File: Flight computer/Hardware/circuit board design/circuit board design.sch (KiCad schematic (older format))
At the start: 0 parts

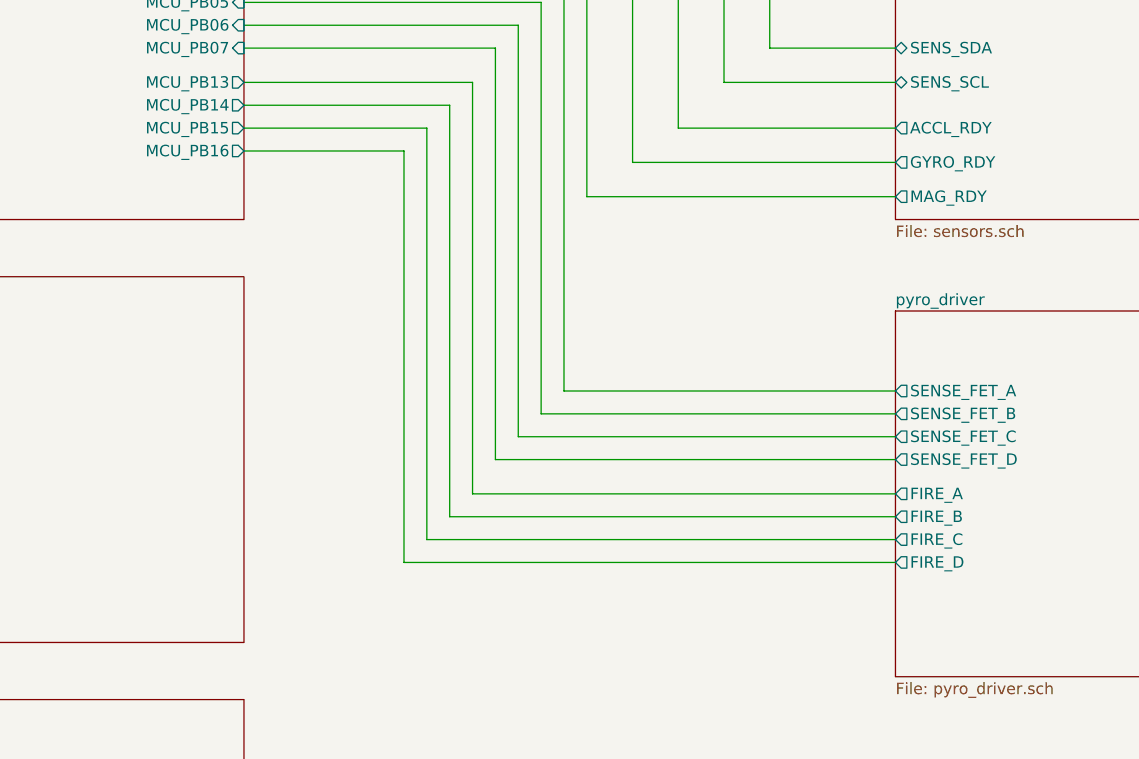
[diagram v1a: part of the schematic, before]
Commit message: added the arming switch. Changed foot print of lipo connector to JST
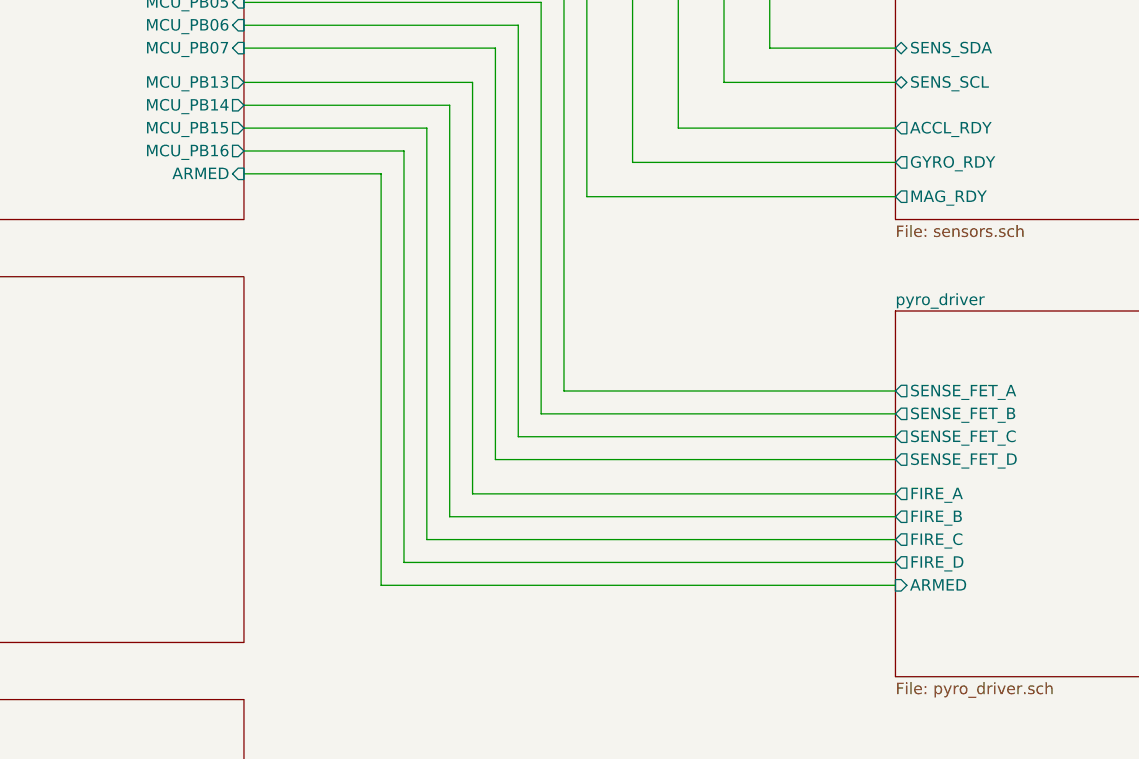
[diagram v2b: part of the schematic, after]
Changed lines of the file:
@@
 F29 "USB_DP" I L 2700 1500 50
 F30 "USB_DM" I L 2700 1400 50
+F31 "ARMED" I R 5050 4100 50
 $EndSheet
 Wire Wire Line
@@
 F8 "SENSE_FET_D" O L 7900 5350 50
 F9 "FIRE_D" O L 7900 5800 50
+F10 "ARMED" I L 7900 5900 50
 $EndSheet
 Wire Wire Line
@@
 Wire Wire Line
 	5050 3550 6150 3550
+Wire Wire Line
+	7900 5900 5650 5900
+Wire Wire Line
+	5650 5900 5650 4100
+Wire Wire Line
+	5650 4100 5050 4100
 $EndSCHEMATC

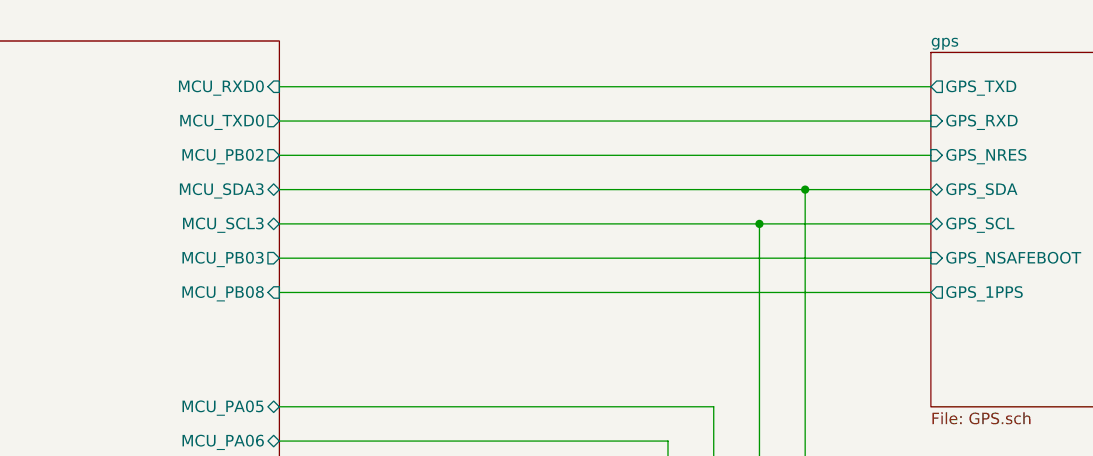
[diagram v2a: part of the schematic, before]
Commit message: changed the SERCOM ports/pins for SPI flash and radio
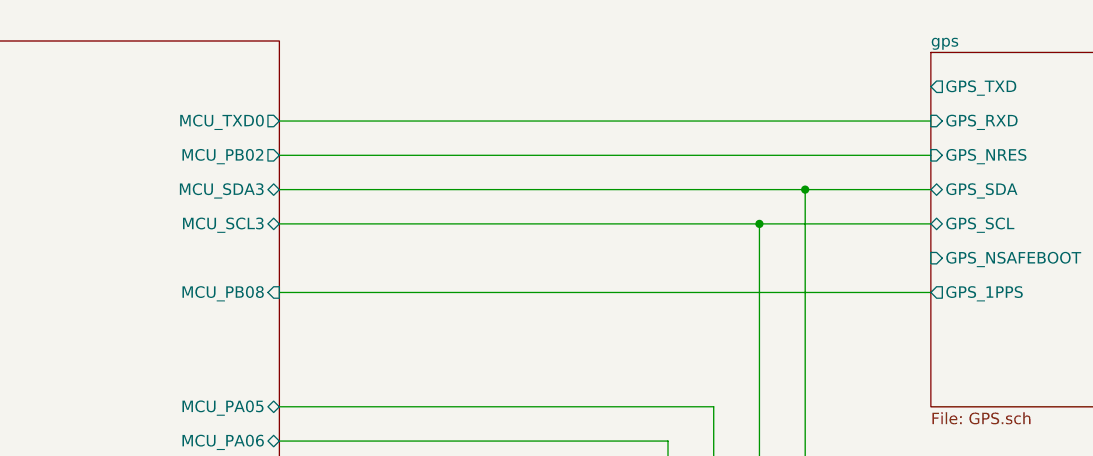
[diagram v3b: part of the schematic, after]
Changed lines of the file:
@@
 	7150 1900 7900 1900
-Wire Wire Line
-	7900 3900 6950 3900
 Wire Wire Line
 	2700 5700 1650 5700
@@
 $EndSheet
 Wire Wire Line
-	7900 4050 6750 4050
-Wire Wire Line
-	6550 3000 6550 4200
-Wire Wire Line
-	6750 4050 6750 2850
-Wire Wire Line
-	6950 3900 6950 2700
-Wire Wire Line
-	6550 4200 7900 4200
-Wire Wire Line
 	6450 3250 6450 5050
 Wire Wire Line
@@
 	5050 1600 7900 1600
 Wire Wire Line
-	5050 2050 7900 2050
-Wire Wire Line
-	5050 3000 6550 3000
-Wire Wire Line
-	6750 2850 5050 2850
-Wire Wire Line
-	6950 2700 5050 2700
-Wire Wire Line
-	7900 1300 5050 1300
-Wire Wire Line
 	5050 1450 7900 1450
 Wire Wire Line
@@
 Wire Wire Line
 	2450 3300 2450 4950
-$Sheet
-S 2700 1100 2350 3200
-U 5D5B15F7
-F0 "MCU" 50
-F1 "MCU.sch" 50
-F2 "MCU_MOSI1" O L 2700 3000 50
-F3 "MCU_SCLK1" O L 2700 3150 50
-F4 "MCU_NSEL1" I L 2700 3300 50
-F5 "MCU_MISO1" O L 2700 2850 50
-F6 "MCU_SDA3" B R 5050 1750 50
-F7 "MCU_SCL3" B R 5050 1900 50
-F8 "MCU_TXD0" O R 5050 1450 50
-F9 "MCU_RXD0" I R 5050 1300 50
-F10 "MCU_PA02" I L 2700 1600 50
-F11 "MCU_PA05" B R 5050 2700 50
-F12 "MCU_PA06" B R 5050 2850 50
-F13 "MCU_PA07" B R 5050 3000 50
-F14 "MCU_PA09" O L 2700 2700 50
-F15 "MCU_PB03" O R 5050 2050 50
-F16 "MCU_PB02" O R 5050 1600 50
-F17 "MCU_PB08" I R 5050 2200 50
-F18 "MCU_PA20" I L 2700 2250 50
-F19 "MCU_PA21" I L 2700 2400 50
-F20 "MCU_PA27" I L 2700 2550 50
-F21 "MCU_PB04" I R 5050 3250 50
-F22 "MCU_PB05" I R 5050 3350 50
-F23 "MCU_PB13" O R 5050 3700 50
-F24 "MCU_PB14" O R 5050 3800 50
-F25 "MCU_PB06" I R 5050 3450 50
-F26 "MCU_PB07" I R 5050 3550 50
-F27 "MCU_PB15" O R 5050 3900 50
-F28 "MCU_PB16" O R 5050 4000 50
-F29 "USB_DP" I L 2700 1500 50
-F30 "USB_DM" I L 2700 1400 50
-F31 "ARMED" I R 5050 4100 50
-$EndSheet
 Wire Wire Line
 	1650 2550 2700 2550
@@
 Wire Wire Line
 	5650 4100 5050 4100
+$Sheet
+S 2700 1100 2350 3200
+U 5D5B15F7
+F0 "MCU" 50
+F1 "MCU.sch" 50
+F2 "MCU_MOSI1" O L 2700 3000 50
+F3 "MCU_SCLK1" O L 2700 3150 50
+F4 "MCU_NSEL1" I L 2700 3300 50
+F5 "MCU_MISO1" O L 2700 2850 50
+F6 "MCU_SDA3" B R 5050 1750 50
+F7 "MCU_SCL3" B R 5050 1900 50
+F8 "MCU_TXD0" O R 5050 1450 50
+F9 "MCU_PA02" I L 2700 1600 50
+F10 "MCU_PA05" B R 5050 2700 50
+F11 "MCU_PA06" B R 5050 2850 50
+F12 "MCU_PA07" B R 5050 3000 50
+F13 "MCU_PA09" O L 2700 2700 50
+F14 "MCU_PB02" O R 5050 1600 50
+F15 "MCU_PB08" I R 5050 2200 50
+F16 "MCU_PA20" I L 2700 2250 50
+F17 "MCU_PA21" I L 2700 2400 50
+F18 "MCU_PA27" I L 2700 2550 50
+F19 "MCU_PB04" I R 5050 3250 50
+F20 "MCU_PB05" I R 5050 3350 50
+F21 "MCU_PB13" O R 5050 3700 50
+F22 "MCU_PB14" O R 5050 3800 50
+F23 "MCU_PB06" I R 5050 3450 50
+F24 "MCU_PB07" I R 5050 3550 50
+F25 "MCU_PB15" O R 5050 3900 50
+F26 "MCU_PB16" O R 5050 4000 50
+F27 "USB_DP" I L 2700 1500 50
+F28 "USB_DM" I L 2700 1400 50
+F29 "ARMED" I R 5050 4100 50
+$EndSheet
+Wire Wire Line
+	6550 4200 7900 4200
+Wire Wire Line
+	6950 3900 6950 2700
+Wire Wire Line
+	6750 4050 6750 2850
+Wire Wire Line
+	6550 3000 6550 4200
+Wire Wire Line
+	7900 4050 6750 4050
+Wire Wire Line
+	7900 3900 6950 3900
+Wire Wire Line
+	6950 2700 5050 2700
+Wire Wire Line
+	6750 2850 5050 2850
+Wire Wire Line
+	5050 3000 6550 3000
 $EndSCHEMATC

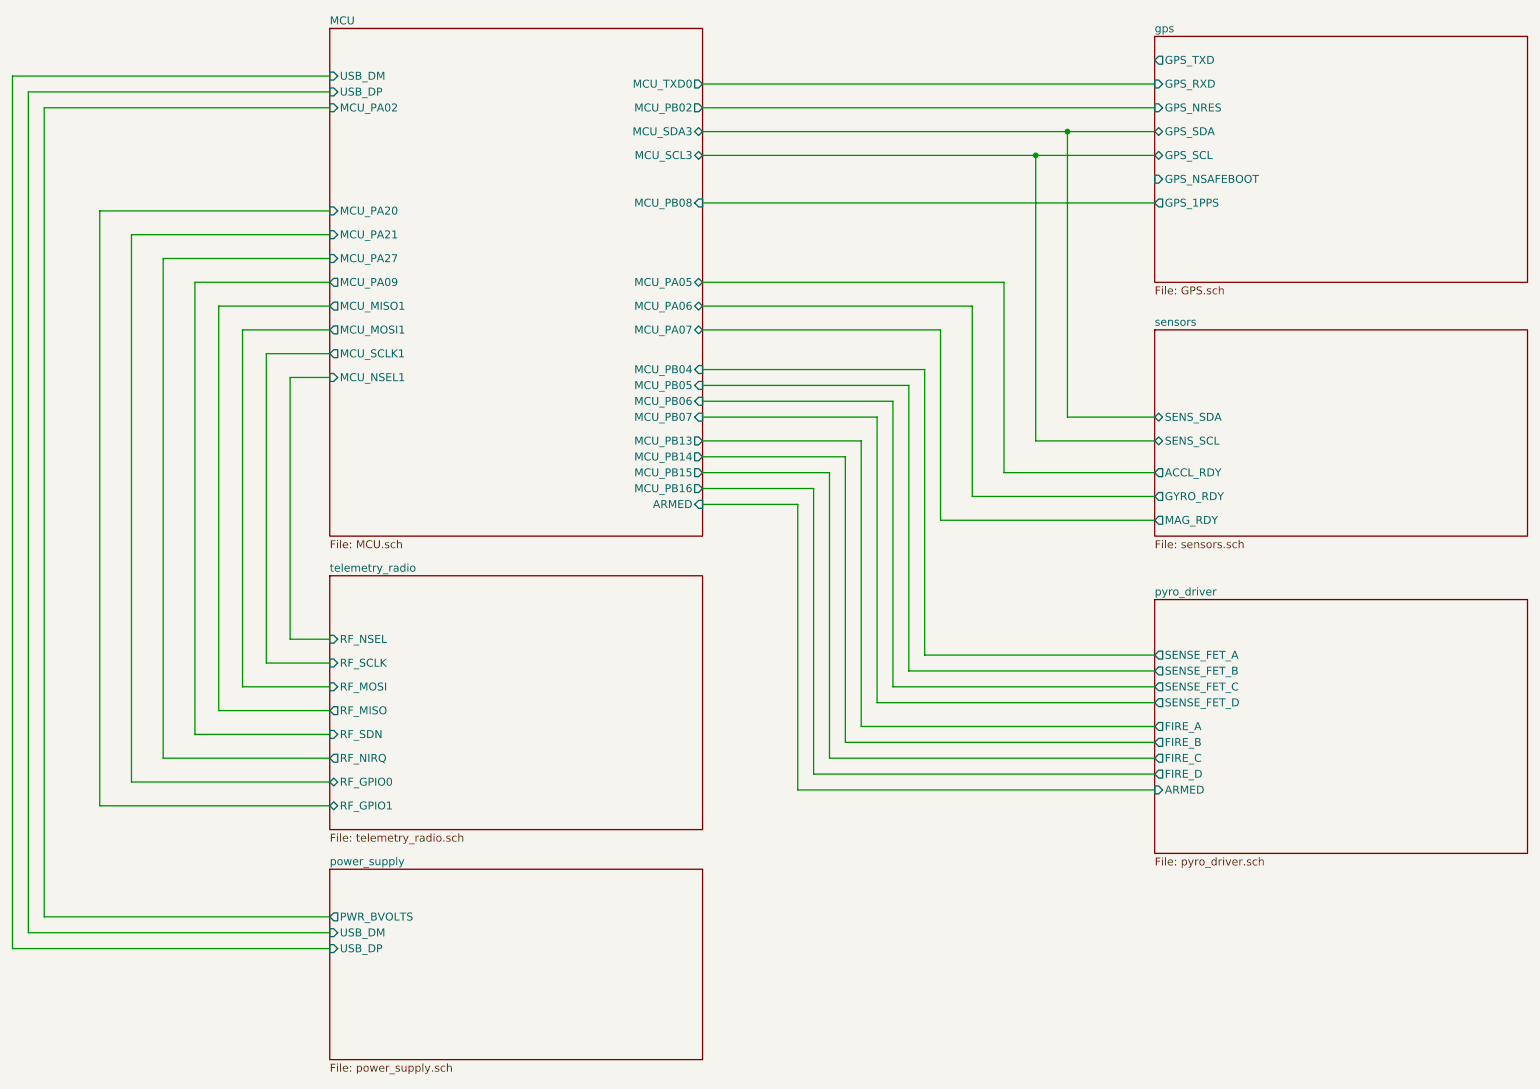
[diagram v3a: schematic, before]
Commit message: Did Major reworking of ports
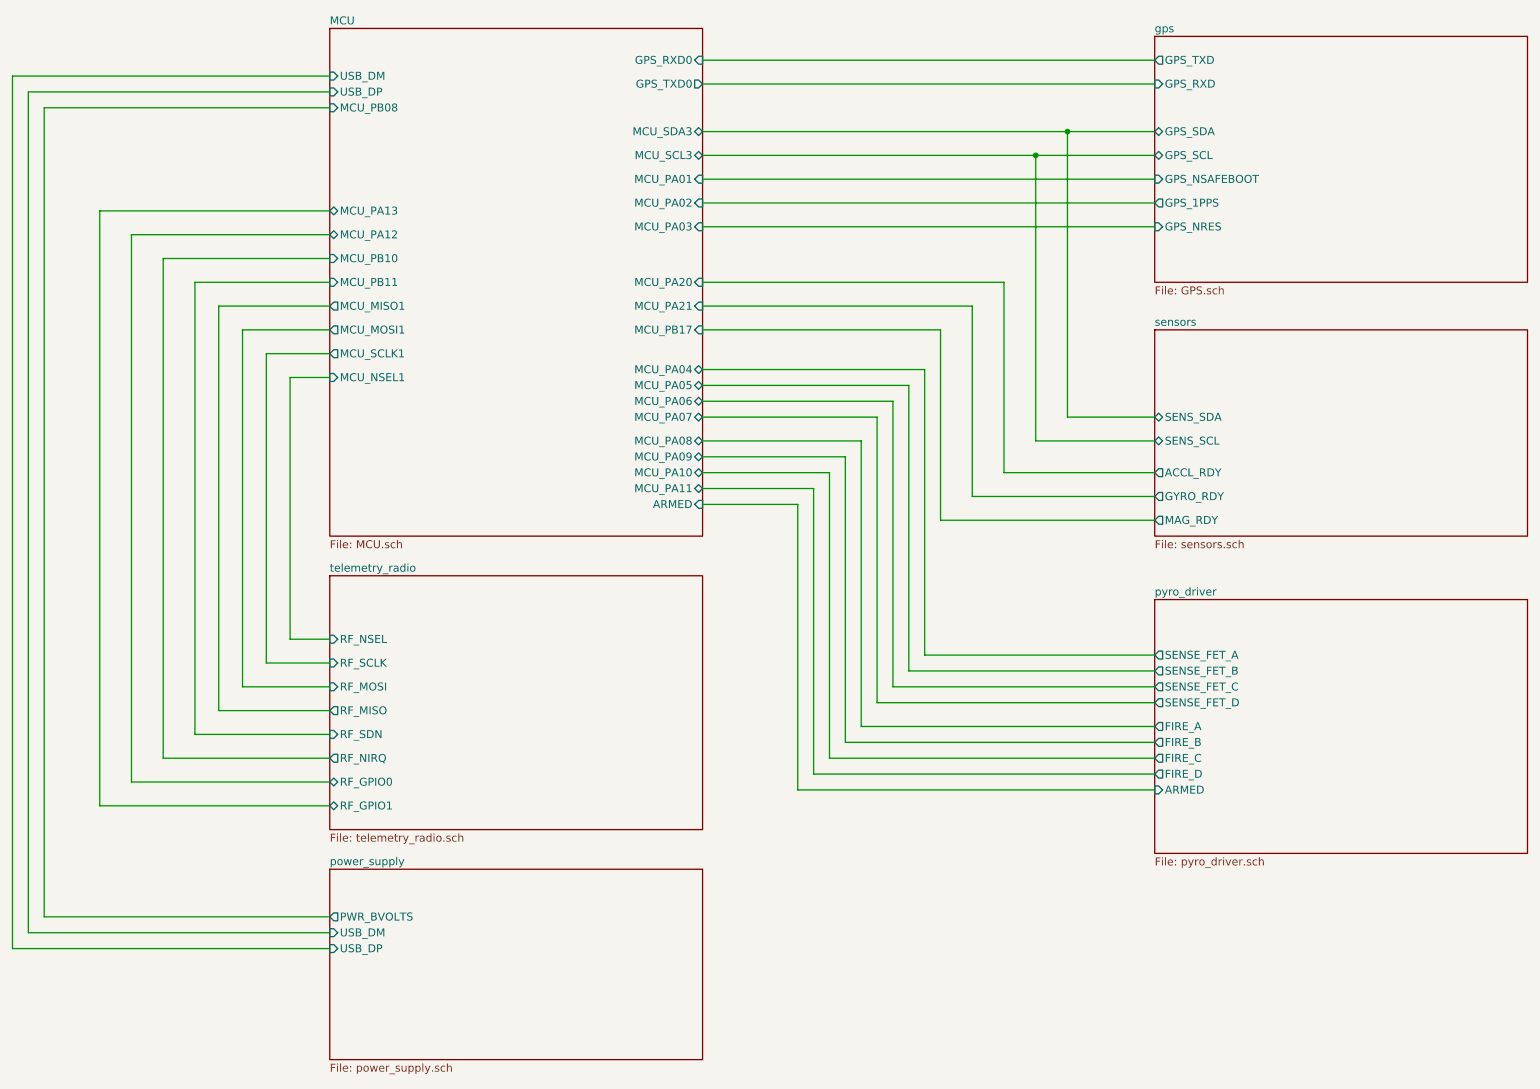
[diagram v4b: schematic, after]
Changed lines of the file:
@@
 F5 "GPS_RXD" I L 7900 1450 50
 F6 "GPS_NSAFEBOOT" I L 7900 2050 50
-F7 "GPS_NRES" I L 7900 1600 50
+F7 "GPS_NRES" I L 7900 2350 50
 F8 "GPS_1PPS" O L 7900 2200 50
 $EndSheet
@@
 	5050 3250 6450 3250
 Wire Wire Line
-	7900 2200 5050 2200
-Wire Wire Line
-	5050 1600 7900 1600
-Wire Wire Line
 	5050 1450 7900 1450
 Wire Wire Line
@@
 	1850 2700 2700 2700
 Wire Wire Line
-	2000 2850 2700 2850
-Wire Wire Line
 	2150 3000 2700 3000
 Wire Wire Line
@@
 Wire Wire Line
 	1650 5700 1650 2550
-Wire Wire Line
-	2000 5400 2000 2850
 Wire Wire Line
 	2150 5250 2150 3000
@@
 Wire Wire Line
 	5650 4100 5050 4100
+Wire Wire Line
+	6550 4200 7900 4200
+Wire Wire Line
+	6950 3900 6950 2700
+Wire Wire Line
+	6750 4050 6750 2850
+Wire Wire Line
+	6550 3000 6550 4200
+Wire Wire Line
+	7900 4050 6750 4050
+Wire Wire Line
+	7900 3900 6950 3900
+Wire Wire Line
+	6950 2700 5050 2700
+Wire Wire Line
+	6750 2850 5050 2850
+Wire Wire Line
+	5050 3000 6550 3000
+Wire Wire Line
+	5050 1300 7900 1300
+Wire Wire Line
+	2000 2850 2700 2850
+Wire Wire Line
+	2000 2850 2000 5400
+Wire Wire Line
+	5050 2050 7900 2050
+Wire Wire Line
+	7900 2200 5050 2200
+Wire Wire Line
+	5050 2350 7900 2350
 $Sheet
 S 2700 1100 2350 3200
@@
 F6 "MCU_SDA3" B R 5050 1750 50
 F7 "MCU_SCL3" B R 5050 1900 50
-F8 "MCU_TXD0" O R 5050 1450 50
-F9 "MCU_PA02" I L 2700 1600 50
-F10 "MCU_PA05" B R 5050 2700 50
-F11 "MCU_PA06" B R 5050 2850 50
-F12 "MCU_PA07" B R 5050 3000 50
-F13 "MCU_PA09" O L 2700 2700 50
-F14 "MCU_PB02" O R 5050 1600 50
-F15 "MCU_PB08" I R 5050 2200 50
-F16 "MCU_PA20" I L 2700 2250 50
-F17 "MCU_PA21" I L 2700 2400 50
-F18 "MCU_PA27" I L 2700 2550 50
-F19 "MCU_PB04" I R 5050 3250 50
-F20 "MCU_PB05" I R 5050 3350 50
-F21 "MCU_PB13" O R 5050 3700 50
-F22 "MCU_PB14" O R 5050 3800 50
-F23 "MCU_PB06" I R 5050 3450 50
-F24 "MCU_PB07" I R 5050 3550 50
-F25 "MCU_PB15" O R 5050 3900 50
-F26 "MCU_PB16" O R 5050 4000 50
-F27 "USB_DP" I L 2700 1500 50
-F28 "USB_DM" I L 2700 1400 50
-F29 "ARMED" I R 5050 4100 50
-$EndSheet
-Wire Wire Line
-	6550 4200 7900 4200
-Wire Wire Line
-	6950 3900 6950 2700
-Wire Wire Line
-	6750 4050 6750 2850
-Wire Wire Line
-	6550 3000 6550 4200
-Wire Wire Line
-	7900 4050 6750 4050
-Wire Wire Line
-	7900 3900 6950 3900
-Wire Wire Line
-	6950 2700 5050 2700
-Wire Wire Line
-	6750 2850 5050 2850
-Wire Wire Line
-	5050 3000 6550 3000
+F8 "MCU_PA02" I R 5050 2200 50
+F9 "MCU_PA05" B R 5050 3350 50
+F10 "MCU_PA06" B R 5050 3450 50
+F11 "MCU_PA07" B R 5050 3550 50
+F12 "MCU_PA20" I R 5050 2700 50
+F13 "MCU_PA21" I R 5050 2850 50
+F14 "USB_DP" I L 2700 1500 50
+F15 "USB_DM" I L 2700 1400 50
+F16 "ARMED" I R 5050 4100 50
+F17 "GPS_TXD0" O R 5050 1450 50
+F18 "GPS_RXD0" I R 5050 1300 50
+F19 "MCU_PA08" B R 5050 3700 50
+F20 "MCU_PA09" B R 5050 3800 50
+F21 "MCU_PA10" B R 5050 3900 50
+F22 "MCU_PA11" B R 5050 4000 50
+F23 "MCU_PA04" B R 5050 3250 50
+F24 "MCU_PA12" B L 2700 2400 50
+F25 "MCU_PA13" B L 2700 2250 50
+F26 "MCU_PB11" I L 2700 2700 50
+F27 "MCU_PB17" I R 5050 3000 50
+F28 "MCU_PB08" I L 2700 1600 50
+F29 "MCU_PA01" I R 5050 2050 50
+F30 "MCU_PA03" I R 5050 2350 50
+F31 "MCU_PB10" I L 2700 2550 50
+$EndSheet
 $EndSCHEMATC

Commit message: Done extensive routing of the board.
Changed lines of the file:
@@
 Wire Wire Line
 	5050 3450 6250 3450
-$Sheet
-S 7900 4700 2350 1600
-U 5D6468D5
-F0 "pyro_driver" 50
-F1 "pyro_driver.sch" 50
-F2 "SENSE_FET_A" O L 7900 5050 50
-F3 "FIRE_A" O L 7900 5500 50
-F4 "SENSE_FET_B" O L 7900 5150 50
-F5 "FIRE_B" O L 7900 5600 50
-F6 "SENSE_FET_C" O L 7900 5250 50
-F7 "FIRE_C" O L 7900 5700 50
-F8 "SENSE_FET_D" O L 7900 5350 50
-F9 "FIRE_D" O L 7900 5800 50
-F10 "ARMED" I L 7900 5900 50
-$EndSheet
 Wire Wire Line
 	5950 5600 5950 3800
@@
 F22 "MCU_PA11" B R 5050 4000 50
 F23 "MCU_PA04" B R 5050 3250 50
-F24 "MCU_PA12" B L 2700 2400 50
-F25 "MCU_PA13" B L 2700 2250 50
+F24 "MCU_PA12" B L 2700 2250 50
+F25 "MCU_PA13" B L 2700 2400 50
 F26 "MCU_PB11" I L 2700 2700 50
 F27 "MCU_PB17" I R 5050 3000 50
@@
 F31 "MCU_PB10" I L 2700 2550 50
 $EndSheet
+$Sheet
+S 7900 4700 2350 1600
+U 5D6468D5
+F0 "pyro_driver" 50
+F1 "pyro_driver.sch" 50
+F2 "SENSE_FET_A" O L 7900 5050 50
+F3 "FIRE_A" O L 7900 5700 50
+F4 "SENSE_FET_B" O L 7900 5150 50
+F5 "FIRE_B" O L 7900 5800 50
+F6 "SENSE_FET_C" O L 7900 5250 50
+F7 "FIRE_C" O L 7900 5500 50
+F8 "SENSE_FET_D" O L 7900 5350 50
+F9 "FIRE_D" O L 7900 5600 50
+F10 "ARMED" I L 7900 5900 50
+$EndSheet
 $EndSCHEMATC

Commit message: only 2 or 3 connections left to route
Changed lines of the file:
@@
 	5050 3550 6150 3550
-Wire Wire Line
-	7900 5900 5650 5900
-Wire Wire Line
-	5650 5900 5650 4100
-Wire Wire Line
-	5650 4100 5050 4100
 Wire Wire Line
 	6550 4200 7900 4200
@@
 F14 "USB_DP" I L 2700 1500 50
 F15 "USB_DM" I L 2700 1400 50
-F16 "ARMED" I R 5050 4100 50
-F17 "GPS_TXD0" O R 5050 1450 50
-F18 "GPS_RXD0" I R 5050 1300 50
-F19 "MCU_PA08" B R 5050 3700 50
-F20 "MCU_PA09" B R 5050 3800 50
-F21 "MCU_PA10" B R 5050 3900 50
-F22 "MCU_PA11" B R 5050 4000 50
-F23 "MCU_PA04" B R 5050 3250 50
-F24 "MCU_PA12" B L 2700 2250 50
-F25 "MCU_PA13" B L 2700 2400 50
-F26 "MCU_PB11" I L 2700 2700 50
-F27 "MCU_PB17" I R 5050 3000 50
-F28 "MCU_PB08" I L 2700 1600 50
-F29 "MCU_PA01" I R 5050 2050 50
-F30 "MCU_PA03" I R 5050 2350 50
-F31 "MCU_PB10" I L 2700 2550 50
+F16 "GPS_TXD0" O R 5050 1450 50
+F17 "GPS_RXD0" I R 5050 1300 50
+F18 "MCU_PA08" B R 5050 3700 50
+F19 "MCU_PA09" B R 5050 3800 50
+F20 "MCU_PA10" B R 5050 3900 50
+F21 "MCU_PA11" B R 5050 4000 50
+F22 "MCU_PA04" B R 5050 3250 50
+F23 "MCU_PA12" B L 2700 2250 50
+F24 "MCU_PA13" B L 2700 2400 50
+F25 "MCU_PB11" I L 2700 2700 50
+F26 "MCU_PB17" I R 5050 3000 50
+F27 "MCU_PB08" I L 2700 1600 50
+F28 "MCU_PA01" I R 5050 2050 50
+F29 "MCU_PA03" I R 5050 2350 50
+F30 "MCU_PB10" I L 2700 2550 50
 $EndSheet
 $Sheet
@@
 F8 "SENSE_FET_D" O L 7900 5350 50
 F9 "FIRE_D" O L 7900 5600 50
-F10 "ARMED" I L 7900 5900 50
 $EndSheet
 $EndSCHEMATC
